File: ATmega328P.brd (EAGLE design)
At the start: 58.4 x 60.6 mm, 13 parts, among them IC1 MEGA8-P, Q1 16MHz

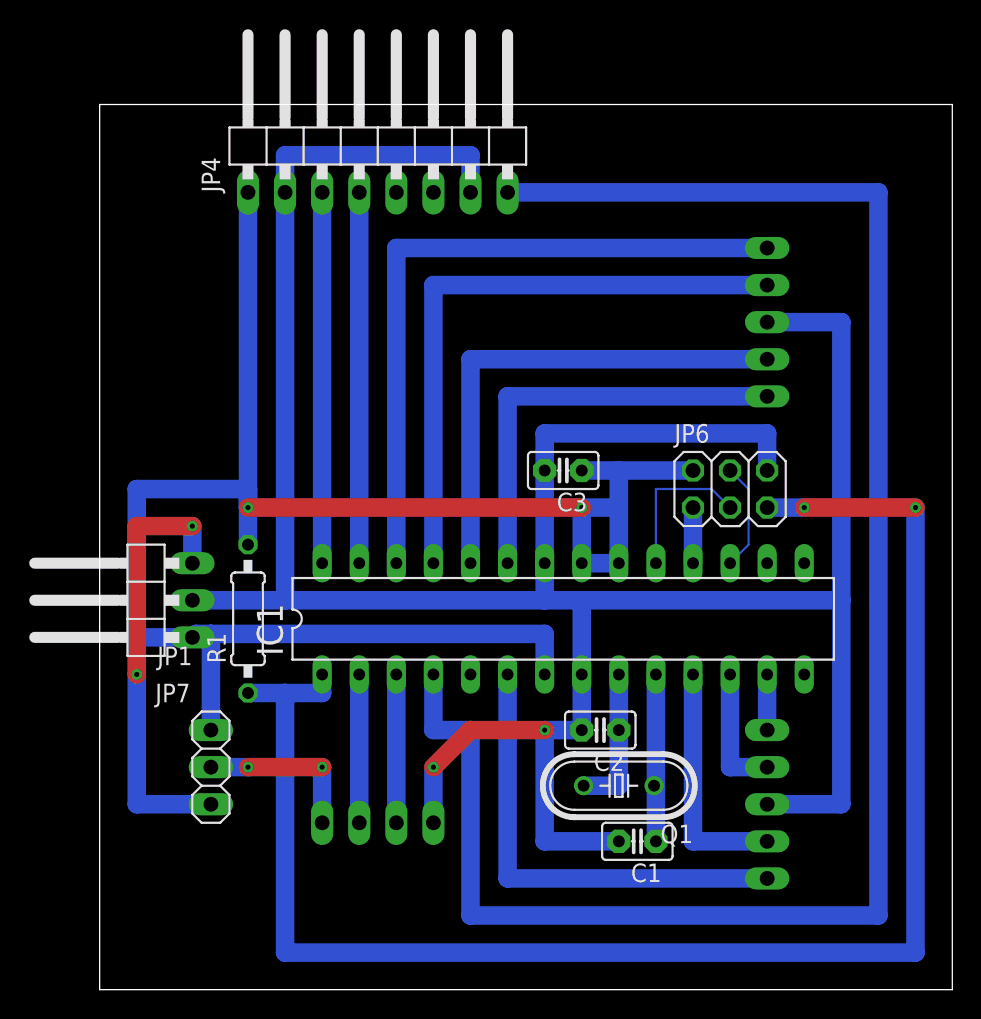
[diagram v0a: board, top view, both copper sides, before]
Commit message: Updated layout
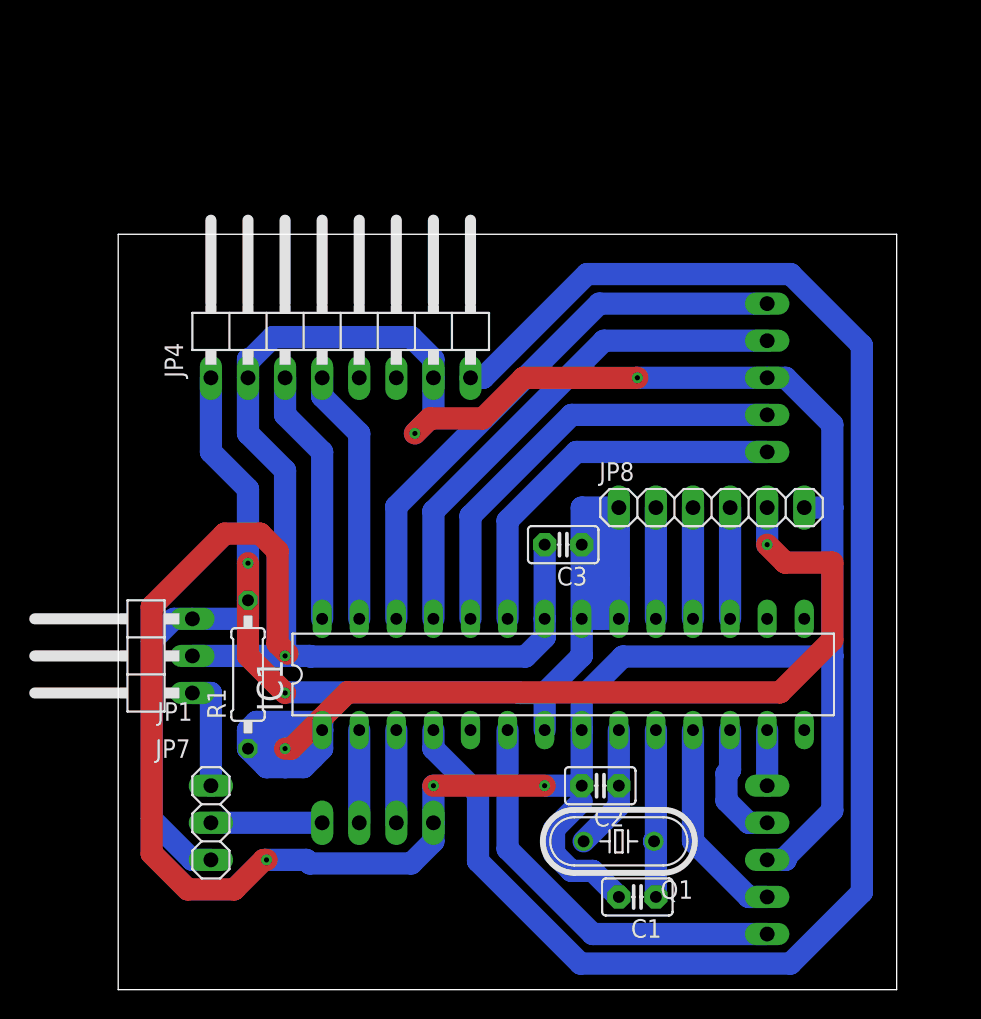
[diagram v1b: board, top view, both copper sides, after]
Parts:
- removed JP6: (no value), pinhead:2X03
- added JP8: (no value), pinhead:1X06
- moved JP4 13.0 mm to (16.5, 45.7)
- moved C3 5.08 mm to (31.8, 30.5)
- moved JP1 3.81 mm to (2.54, 22.9)
- moved JP2 3.81 mm to (49.5, 41.9)
- moved C1 3.81 mm to (36.8, 6.35)
- moved C2 3.81 mm to (34.3, 14.0)
- moved JP7 3.81 mm to (7.62, 11.4)
- moved Q1 3.81 mm to (35.6, 10.2)
- moved IC1 3.81 mm to (31.8, 21.6)
- moved JP3 3.81 mm to (49.5, 8.89)
- moved R1 3.81 mm to (10.2, 21.6)
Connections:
- net 3V3: now also JP1.1, JP7.1; no longer JP1.3, JP7.3
- net 5V: now also JP1.3, JP7.3, JP8.1; no longer JP1.1, JP6.2, JP7.1
- net GND: now also JP8.6; no longer JP6.6
- net N$4: now also JP8.3; no longer JP6.1
- net N$7: now also JP8.4; no longer JP6.4
- net N$8: now also JP8.2; no longer JP6.3
- net N$9: now also JP8.5; no longer JP6.5
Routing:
- net GND: track 199.2 -> 243.5 mm, vias 2 -> 6
- net N$9: track 108.0 -> 81.2 mm
- net 3V3: track 30.5 -> 7.62 mm, vias 2 -> 0
- net 5V: track 126.3 -> 110.4 mm
- net INT: track 121.9 -> 110.7 mm
- net B2: track 47.0 -> 38.8 mm
- net SDA: track 25.4 -> 17.6 mm
- net SCL: track 25.4 -> 17.6 mm
- net B1: track 41.9 -> 35.1 mm
- net A2: track 34.3 -> 30.2 mm
- net N$4: track 3.81 -> 7.62 mm
- net N$3: track 11.4 -> 7.62 mm, vias 2 -> 0
- net TX: track 10.2 -> 6.35 mm
- net RX: track 10.2 -> 6.35 mm
- net C1: track 31.7 -> 28.3 mm
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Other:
- board size 58.4 x 60.6 mm -> 53.3 x 51.7 mm

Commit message: Some adjustments to ISP, pin order matches arduino ISP
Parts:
- JP8: device pinhead:1X06 -> pinhead:1X05
- moved JP4 6.35 mm to (12.7, 40.6)
- moved JP8 4.02 mm to (40.6, 29.2), turned to 180 degrees
- moved JP2 2.54 mm to (49.5, 39.4)
- moved JP5 1.27 mm to (19.1, 6.35)
- moved C3 1.27 mm to (31.8, 29.2)
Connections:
- removed net N$8: IC1.19, JP8.2
- new net N$5: IC1.19, JP8.4
- net 5V: no longer JP8.1
- net GND: now also JP8.5; no longer JP8.6
- net N$7: now also JP8.2; no longer JP8.4
- net N$9: now also JP8.1; no longer JP8.5
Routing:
- net GND: track 243.5 -> 280.6 mm
- net 5V: track 110.4 -> 130.7 mm
- net N$8: track 7.62 -> 0.00 mm
- net N$9: track 81.2 -> 76.9 mm
- net N$7: track 7.62 -> 3.81 mm
- net N$6: track 7.62 -> 3.81 mm
- net N$5: track 0.00 -> 3.81 mm
- net INT: track 110.7 -> 113.0 mm
- net B2: track 38.8 -> 37.0 mm
- net B1: track 35.1 -> 33.2 mm
- net A2: track 30.2 -> 28.4 mm
- net A1: track 26.5 -> 24.6 mm
- net SCL: track 17.6 -> 15.7 mm
- net SDA: track 17.6 -> 16.1 mm
- net N$3: track 7.62 -> 8.89 mm
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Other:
- board size 53.3 x 51.7 mm -> 53.3 x 49.2 mm
